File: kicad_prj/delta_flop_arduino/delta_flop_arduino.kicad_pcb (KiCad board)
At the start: 2 copper layers, 94.4 x 55.6 mm, 14 parts, among them J1 SD_Card, J2 SCREEN OUTPUT, J3 Power Input (5V), SW1 RotaryEncoder_Switch, U1 Arduino_Nano

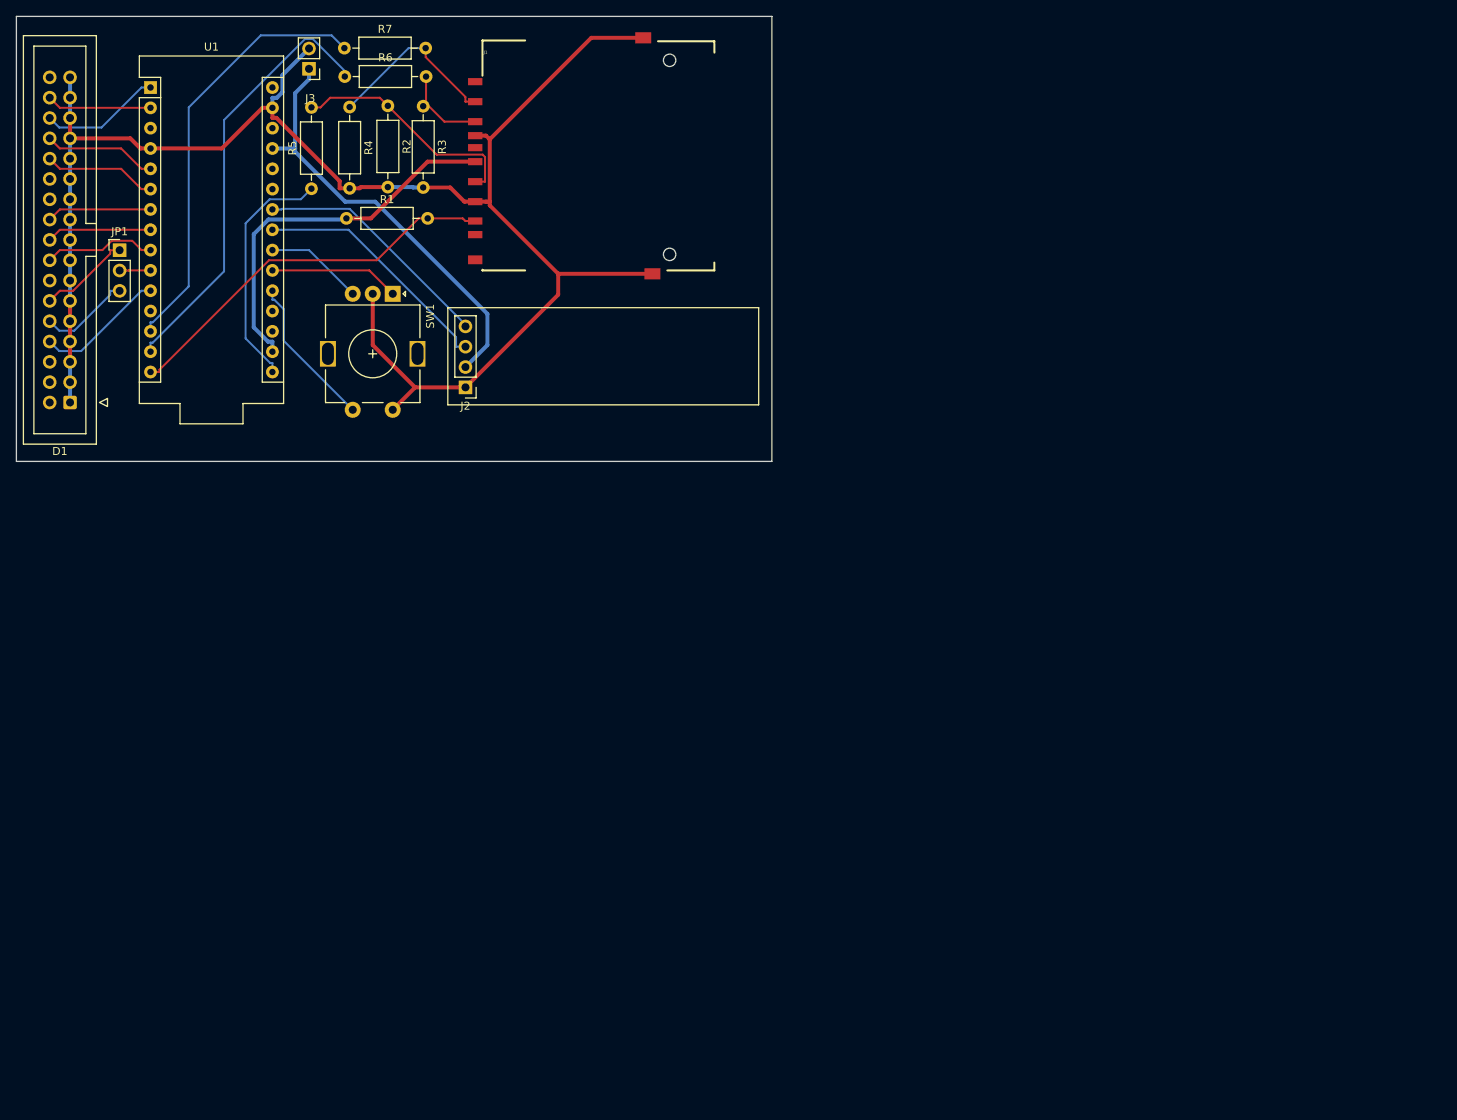
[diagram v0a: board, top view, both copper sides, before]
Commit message: Big screen update
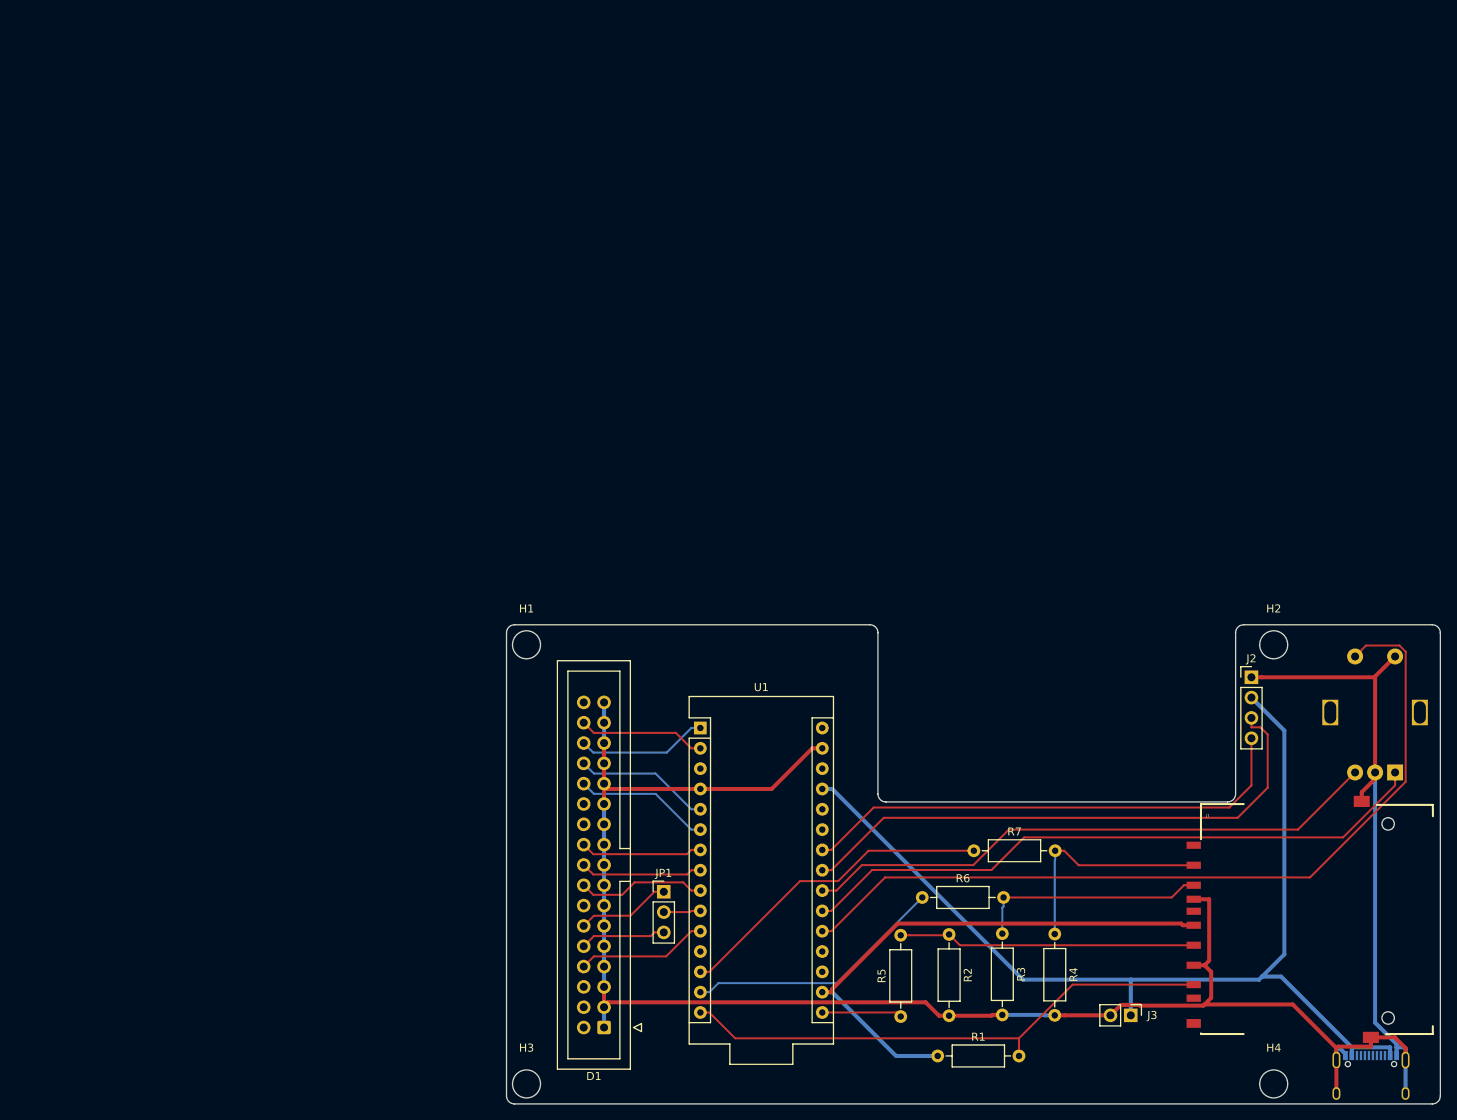
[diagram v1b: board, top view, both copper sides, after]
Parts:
- added H1: MountingHole_3.5mm, MountingHole:MountingHole_3.5mm, F.Cu at (105.8, 104.0)
- added H2: MountingHole_3.5mm, MountingHole:MountingHole_3.5mm, F.Cu at (199.2, 104.0)
- added H3: MountingHole_3.5mm, MountingHole:MountingHole_3.5mm, F.Cu at (105.8, 158.9)
- added H4: MountingHole_3.5mm, MountingHole:MountingHole_3.5mm, F.Cu at (199.2, 158.9)
- added J4: USB_C_Receptacle_PowerOnly_6P, delta_flop_pre:USB_C_Receptacle_XKB_U262-16XN-4BVC11, B.Cu at (211.3, 159.1)
- SW1: moved to B.Cu
- moved J3 156.7 mm to (181.3, 150.4), turned to -90 degrees
- moved SW1 138.8 mm to (214.3, 120.0), turned to 90 degrees
- moved R4 135.9 mm to (171.8, 140.2)
- moved J1 131.1 mm to (190.2, 138.4)
- moved R1 128.2 mm to (157.2, 155.4)
- moved R7 127.5 mm to (161.7, 129.8)
- moved R5 127.0 mm to (152.6, 150.5)
- moved R3 126.2 mm to (165.3, 140.2)
- moved R6 125.5 mm to (155.2, 135.6)
- moved R2 125.1 mm to (158.6, 140.3)
- moved U1 105.5 mm to (127.5, 114.5)
- moved JP1 105.2 mm to (122.9, 134.9)
- moved J2 104.7 mm to (196.4, 108.1), turned to 0 degrees
- moved D1 102.8 mm to (115.5, 151.9)
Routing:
- net Net-(U1-A1/D15): track 19.2 -> 104.1 mm
- net /5V: track 54.1 -> 128.9 mm
- net GND: track 213.3 -> 282.2 mm
- net Net-(U1-A2/D16): track 16.2 -> 79.7 mm
- net Net-(U1-A3/D17): track 12.3 -> 72.7 mm
- net Net-(J2-Pin_3): track 30.9 -> 70.2 mm
- net Net-(J2-Pin_4): track 30.4 -> 62.9 mm
- net MOSI: track 54.6 -> 32.6 mm
- net /3.3V: track 47.4 -> 68.0 mm
- net SCK: track 30.2 -> 10.0 mm
- net MISO: track 48.8 -> 68.0 mm
- net Net-(J1-CMD): track 10.9 -> 29.0 mm
- net SS: track 54.0 -> 40.5 mm
- net Net-(J1-CLK): track 29.6 -> 37.2 mm
- net Net-(J1-CD/DAT3): track 22.5 -> 28.5 mm
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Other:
- board size 94.4 x 55.6 mm -> 116.7 x 59.9 mm

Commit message: First Gerbers Produced
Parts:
- D1: value Floppy Connector -> 34 Pin Floppy Connector
- U1: value Arduino_Nano -> Arduino Nano
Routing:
- net Net-(U1-A1/D15): track 104.1 -> 107.8 mm
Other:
- board text added: "1 2 3"
- board text added: "Drive A"
- board text added: "Drive B"
- board text added: "Floppy Emulator For ZX Spectrum Beta Disk PCB by MadCat, 2024 Ver.1.0"
